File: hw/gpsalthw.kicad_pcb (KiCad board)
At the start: 2 copper layers, 54.9 x 55.4 mm, 43 parts, among them J1 serial, J2 display, J3 antenna, J4 USB_B_Micro, J5 battery, Q1 IRLML5203TRPBF, Q2 IRLML5203TRPBF, SW1 reset, SW2 boot, SW3 btn-up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

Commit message: схема/плата - добавлены кондецаторы по питанию
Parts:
- added C6: 470 pF, Capacitor_SMD:C_0805_2012Metric, F.Cu at (101.1, 47.0)
- added C7: 1μF, Capacitor_SMD:C_0805_2012Metric, F.Cu at (101.2, 69.4)
- moved R6 1.59 mm to (102.0, 65.0)
- moved R7 1.59 mm to (99.9, 65.0)
- moved R8 1.59 mm to (97.9, 65.0)
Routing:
- net Net-(C6-Pad1): track 0.00 -> 11.4 mm
- net hwpwr: track 8.89 -> 11.7 mm
- net /batt-chk: track 5.86 -> 4.92 mm
- net Net-(R7-Pad2): track 2.85 -> 3.67 mm
- net +BATT: track 39.9 -> 39.4 mm
- net GND: vias 27 -> 28
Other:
- board text added: "GPS-adv v0.3"
- board text removed: "GPS-adv v0.2"

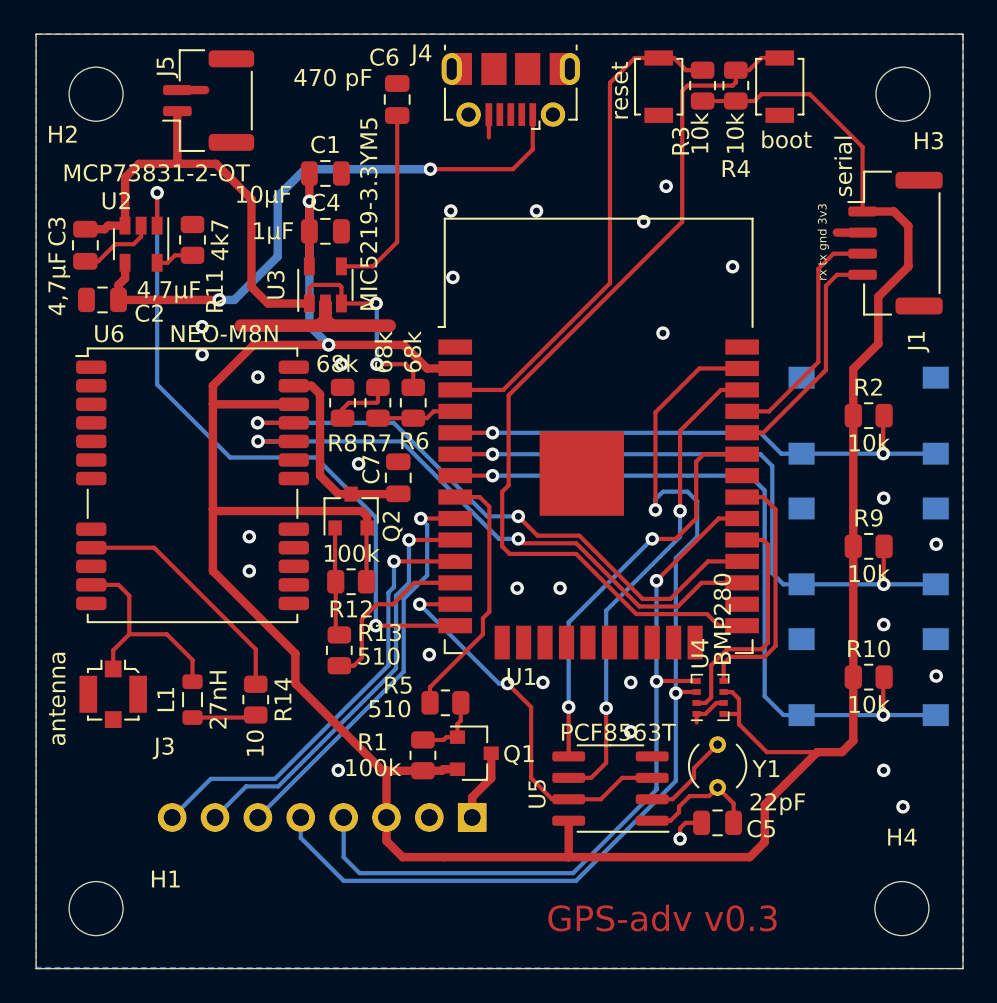
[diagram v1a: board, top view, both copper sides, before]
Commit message: hw - перевернут вовнутрь разъём serial и кнопки заменены на более маленькие
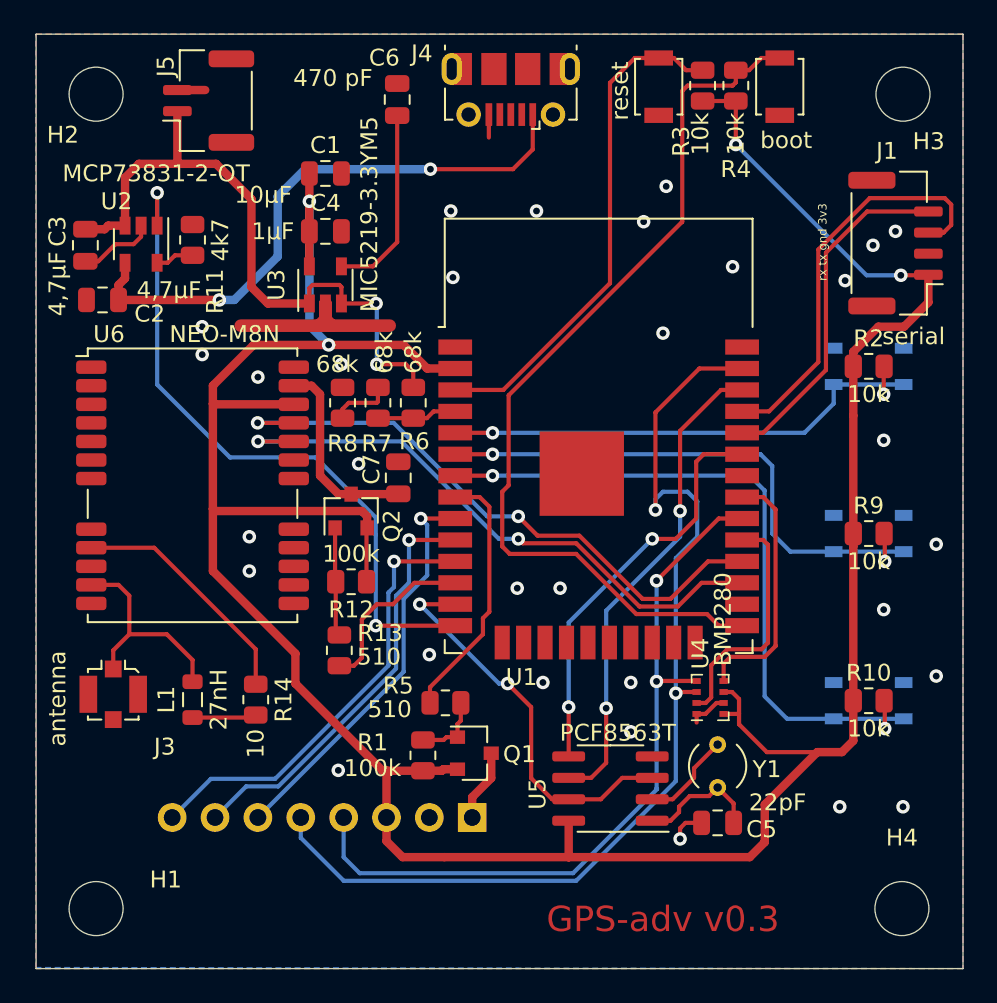
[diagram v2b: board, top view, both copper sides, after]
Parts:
- SW3, SW4, SW5: footprint Button_Switch_SMD:SW_Push_1P1T_NO_6x6mm_H9.5mm -> Button_Switch_SMD:SW_SPST_PTS810
- moved R2 2.92 mm to (129.0, 62.8)
- moved SW3 2.92 mm to (129.0, 62.8)
- moved R10 1.40 mm to (129.0, 82.6)
- moved SW5 1.40 mm to (129.0, 82.6)
- moved R9 0.76 mm to (129.0, 72.7)
- moved SW4 0.76 mm to (129.0, 72.7)
- turned J1 to 90 degrees
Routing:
- net /TX: track 14.6 -> 24.4 mm
- net /RX: track 14.3 -> 20.5 mm
- net /b-sel: track 37.7 -> 33.6 mm
- net GND: track 25.5 -> 23.6 mm, vias 28 -> 31
- net /b-down: track 43.8 -> 41.9 mm
- net /b-up: track 31.3 -> 30.7 mm
- net +3V3: vias 2 -> 4

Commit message: hw - добавлены пвторители кнопок другого размера посадочных мест
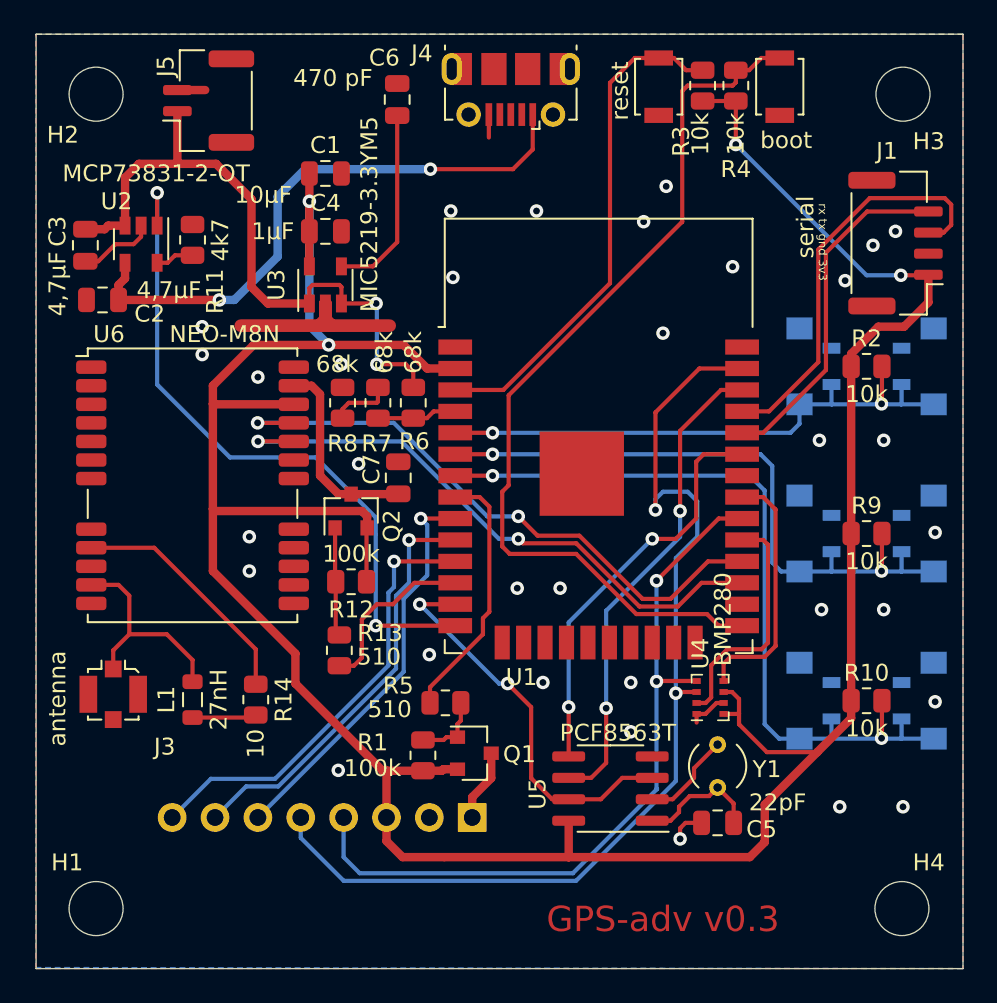
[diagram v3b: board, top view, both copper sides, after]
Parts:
- added SW6: btn-up2, Button_Switch_SMD:SW_Push_1P1T_NO_6x6mm_H9.5mm, B.Cu at (128.9, 62.8)
- added SW7: btn-sel2, Button_Switch_SMD:SW_Push_1P1T_NO_6x6mm_H9.5mm, B.Cu at (128.9, 72.7)
- added SW8: btn-down2, Button_Switch_SMD:SW_Push_1P1T_NO_6x6mm_H9.5mm, B.Cu at (128.9, 82.6)
- moved R10 0.13 mm to (128.9, 82.6)
- moved R2 0.13 mm to (128.9, 62.8)
- moved R9 0.13 mm to (128.9, 72.7)
- moved SW3 0.13 mm to (128.9, 62.8)
- moved SW4 0.13 mm to (128.9, 72.7)
- moved SW5 0.13 mm to (128.9, 82.6)
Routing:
- net /b-sel: track 33.6 -> 39.2 mm
- net /b-down: track 41.9 -> 47.6 mm
- net /b-up: track 30.7 -> 34.4 mm
- net +3V3: track 177.1 -> 176.4 mm
- net GND: vias 31 -> 33

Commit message: плата - разъёмы батареи и serial заменены на более правильные
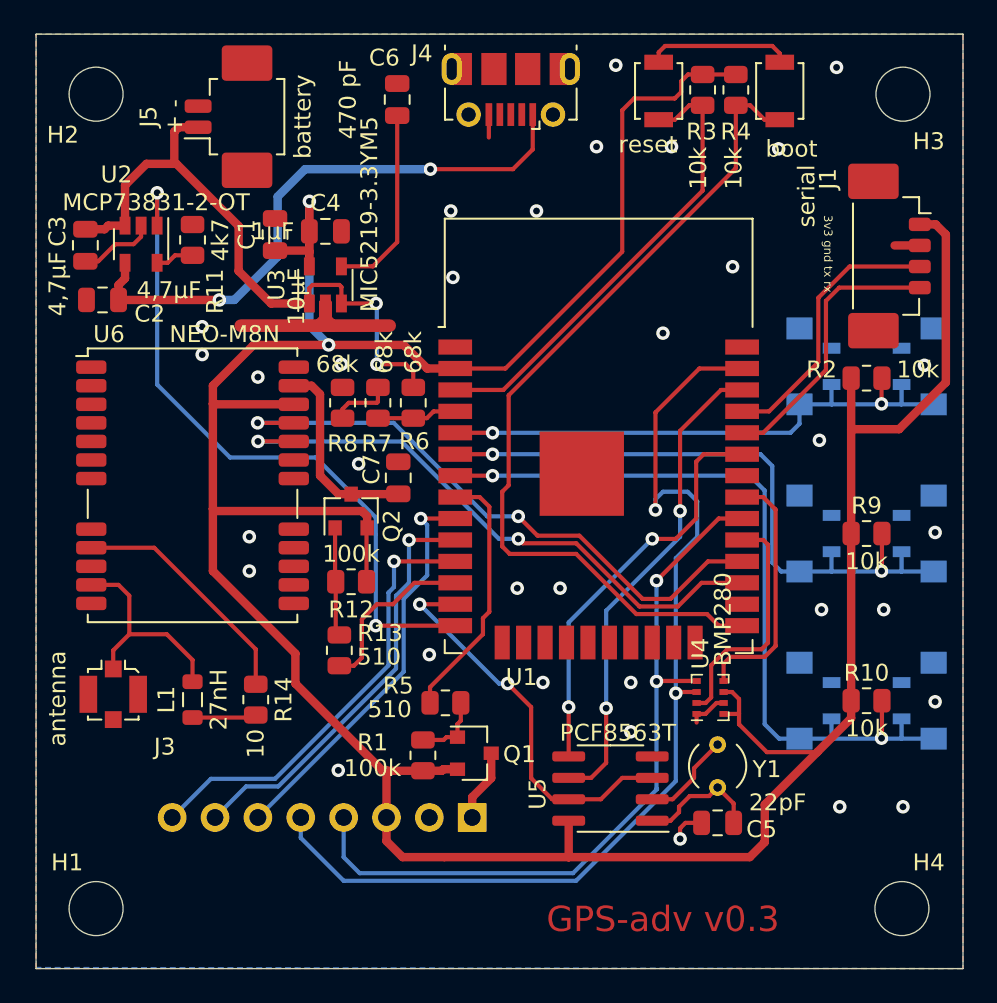
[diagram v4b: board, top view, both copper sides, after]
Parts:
- J1: footprint Connector_JST:JST_GH_BM04B-GHS-TBT_1x04-1MP_P1.25mm_Vertical -> Connector_Molex:Molex_PicoBlade_53398-0471_1x04-1MP_P1.25mm_Vertical
- J5: footprint Connector_JST:JST_GH_SM02B-GHS-TB_1x02-1MP_P1.25mm_Horizontal -> Connector_Molex:Molex_PicoBlade_53261-0271_1x02-1MP_P1.25mm_Horizontal
- moved C1 4.69 mm to (93.9, 55.0), turned to 90 degrees
- moved J5 2.02 mm to (91.7, 48.0)
- moved J1 0.79 mm to (130.8, 56.3), turned to 270 degrees
- moved R2 0.70 mm to (128.9, 63.5)
- moved R3 0.25 mm to (119.2, 46.4), turned to 270 degrees
- moved R4 0.25 mm to (121.2, 46.4), turned to 270 degrees
- moved SW1 0.25 mm to (116.6, 46.5), turned to 270 degrees
- moved SW2 0.25 mm to (123.8, 46.5), turned to 270 degrees
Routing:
- net +3V3: track 176.4 -> 194.7 mm, vias 4 -> 2
- net GND: track 23.6 -> 32.1 mm
- net /TX: track 24.4 -> 16.3 mm
- net /RX: track 20.5 -> 16.5 mm
- net Net-(R4-Pad2): track 54.6 -> 51.0 mm
- net Net-(R3-Pad2): track 30.1 -> 28.0 mm
- net +BATT: track 39.4 -> 37.9 mm
- net /b-up: track 34.4 -> 33.7 mm
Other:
- board text added: "+ -"
- board text added: "3v3 gnd tx rx"
- board text removed: "rx tx gnd 3v3"

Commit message: плата - поправлены кнопки reset/boot
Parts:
- SW1, SW2: footprint Button_Switch_SMD:SW_SPST_B3U-1000P -> Button_Switch_SMD:SW_Push_SPST_NO_Alps_SKRK
- moved SW1 0.54 mm to (116.2, 46.1)
- moved SW2 0.50 mm to (124.1, 46.1)
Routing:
- net GND: track 32.1 -> 23.5 mm, vias 33 -> 32
